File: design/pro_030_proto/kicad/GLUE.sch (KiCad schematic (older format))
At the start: 19 parts, among them IC10 74HCT93, IC11 74LS08, IC12 74HCT93, IC13 74HCT174, IC14 74LS01N, IC9 74174N, X2 8MHz

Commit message: Lots of work
* Sort out power and reset circuits, add ATX
* Add PCF8584 and supporting GAL code
* Stub out ATX board outline in PCB
* Various other tidying up and prep for layout
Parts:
- IC14: value 74LS01N -> 74LS05; symbol rosco_m68k-eagle-import:7401N -> 74xx:74LS05
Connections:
- wire segments 142 -> 139
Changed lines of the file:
@@
 $Descr A4 11693 8268
 encoding utf-8
-Sheet 6 13
+Sheet 6 15
 Title "rosco_m68k Pro (030) Prototype"
-Date "2021-07-24"
+Date "2021-10-01"
 Rev "0"
 Comp "The Really Old-School Company Limited"
@@
 	1950 750  1950 1150
 $Comp
-L rosco_m68k-eagle-import:7401N IC?
+L 74xx:74LS05 IC?
 U 4 1 60F552BD
-P 9950 1700
+P 9950 1600
 AR Path="/60F552BD" Ref="IC?"  Part="3"
 AR Path="/5E53B952/60F552BD" Ref="IC?"  Part="4"
 AR Path="/5E53BC83/60F552BD" Ref="IC?"  Part="4"
 AR Path="/60FBFA5C/60F552BD" Ref="IC14"  Part="4"
-F 0 "IC14" H 10050 1825 59  0000 L BNN
-F 1 "74LS01N" H 10050 1500 59  0001 L BNN
-F 2 "Package_DIP:DIP-14_W7.62mm_Socket_LongPads" H 9950 1700 50  0001 C CNN
-F 3 "" H 9950 1700 50  0001 C CNN
-	4    9950 1700
-	1    0    0    -1
-$EndComp
-Text GLabel 10250 1700 2    50   Output ~ 0
+F 0 "IC14" H 10050 1725 59  0000 L BNN
+F 1 "74LS05" H 10050 1400 59  0001 L BNN
+F 2 "Package_DIP:DIP-14_W7.62mm_Socket_LongPads" H 9950 1600 50  0001 C CNN
+F 3 "" H 9950 1600 50  0001 C CNN
+	4    9950 1600
+	1    0    0    -1
+$EndComp
+Text GLabel 10250 1600 2    50   Output ~ 0
 BERR
 Text Notes 9050 2600 2    50   ~ 0
 DTACK / IACK WATCHDOG
-Wire Wire Line
-	8550 2000 8550 2200
 $Comp
 L power:GND #PWR027
@@
 NoConn ~ 9050 1500
 NoConn ~ 9050 1400
-Connection ~ 9350 1600
-Wire Wire Line
-	9350 1600 9050 1600
-Wire Wire Line
-	9350 1800 9650 1800
-Wire Wire Line
-	9350 1600 9350 1800
-Wire Wire Line
-	9650 1600 9350 1600
 Text GLabel 8050 1300 0    50   Input ~ 0
 CLK_1M
@@
 Wire Wire Line
 	8050 3450 8050 4850
-Wire Wire Line
-	8050 5150 8600 5150
-Wire Wire Line
-	8600 5150 8600 4950
 $Comp
 L power:GND #PWR028
@@
 	1    0    0    -1
 $EndComp
-Connection ~ 8600 5150
 $Comp
 L power:VCC #PWR025
@@
 NoConn ~ 6100 6350
 NoConn ~ 6100 6950
+Wire Wire Line
+	9050 1600 9650 1600
+Wire Wire Line
+	8050 5150 8600 5150
+Wire Wire Line
+	8600 5150 8600 4950
+Connection ~ 8600 5150
+Wire Wire Line
+	8550 2200 8550 2000
 $EndSCHEMATC

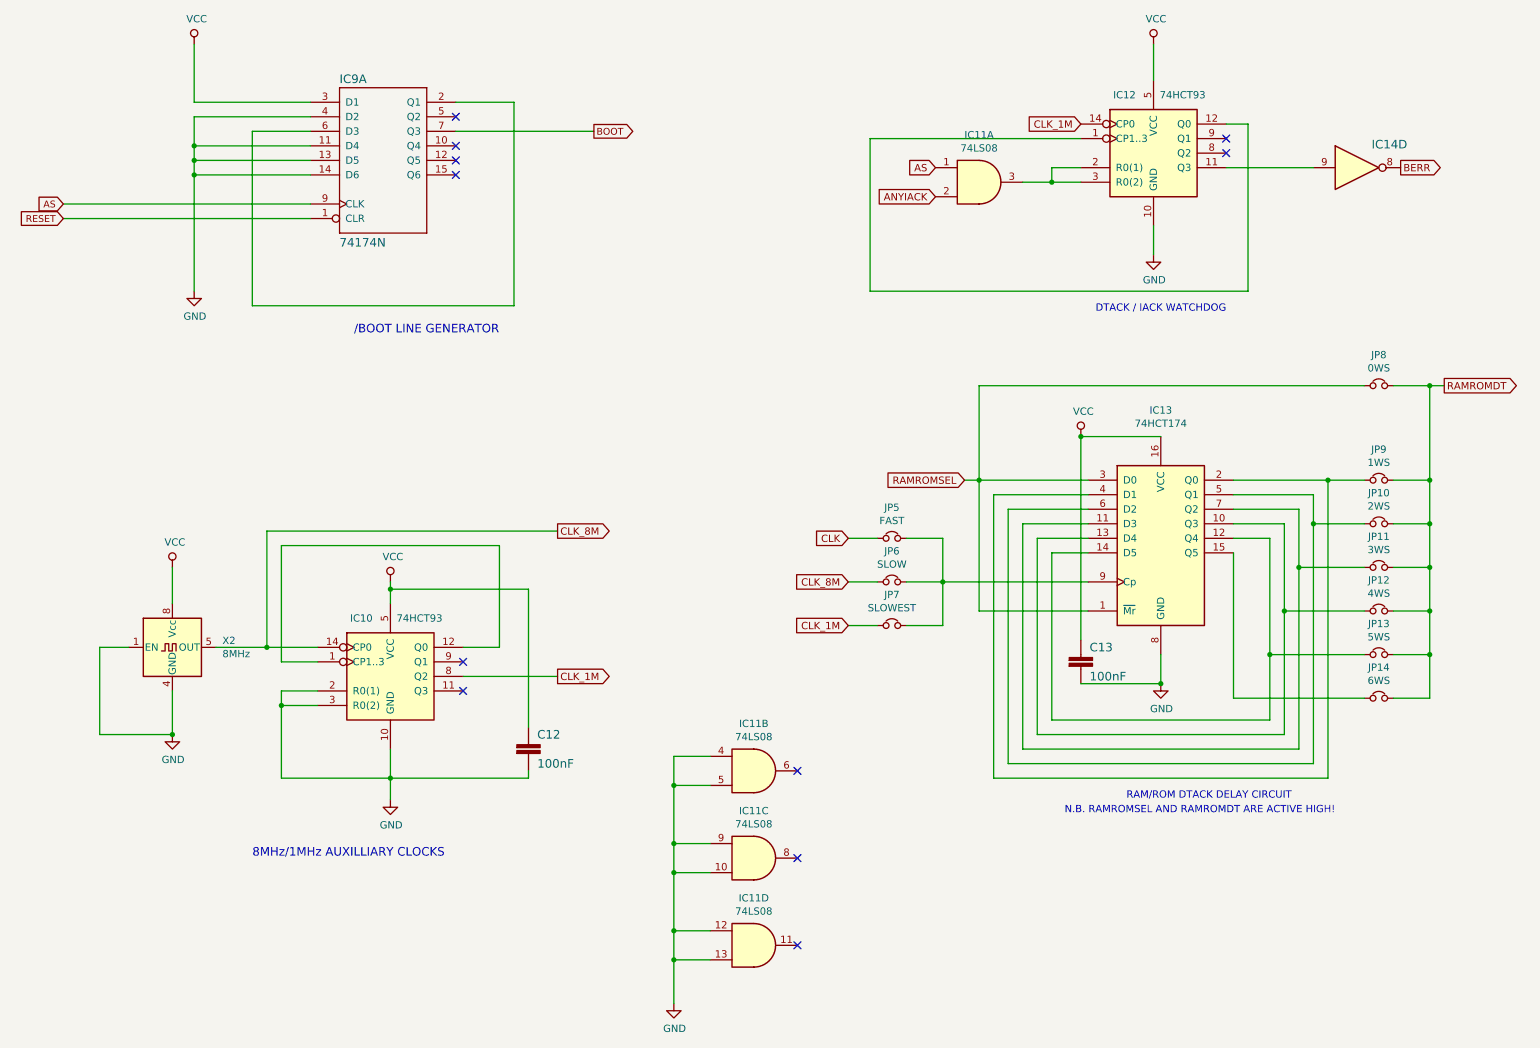
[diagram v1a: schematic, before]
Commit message: Replace 7493s and 7404 with IC10 GAL
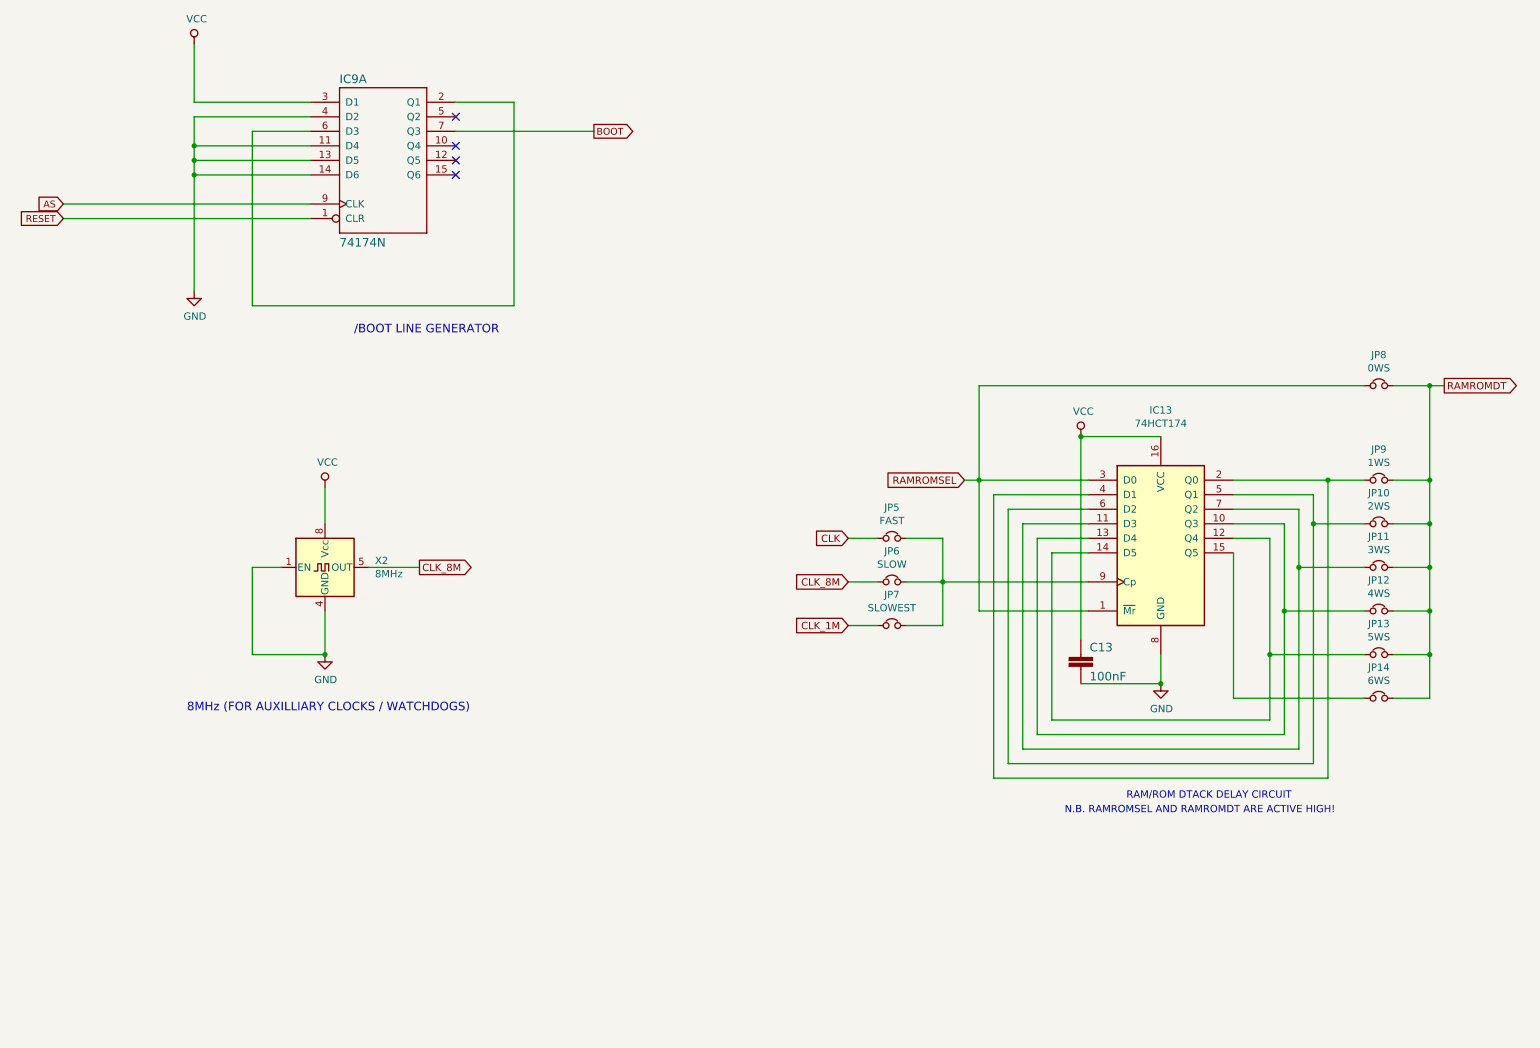
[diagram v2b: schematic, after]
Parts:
- removed C12: 100nF, Capacitor_THT:C_Rect_L4.0mm_W2.5mm_P2.50mm, symbol rosco_m68k-eagle-import:C2,5-3
- removed IC10, IC12: 74HCT93, Package_DIP:DIP-14_W7.62mm_Socket_LongPads, symbol 74xx:74LS93
- removed IC11: 74LS08, Package_DIP:DIP-14_W7.62mm_LongPads, symbol 74xx:74LS08
- removed IC14: 74LS05, Package_DIP:DIP-14_W7.62mm_Socket_LongPads, symbol 74xx:74LS05
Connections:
- no-connect marks 11 -> 4
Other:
- note added: "8MHz (FOR AUXILLIARY CLOCKS / WATCHDOGS)"
- note removed: "8MHz/1MHz AUXILLIARY CLOCKS"
- note removed: "DTACK / IACK WATCHDOG"
- moved on the sheet: X2

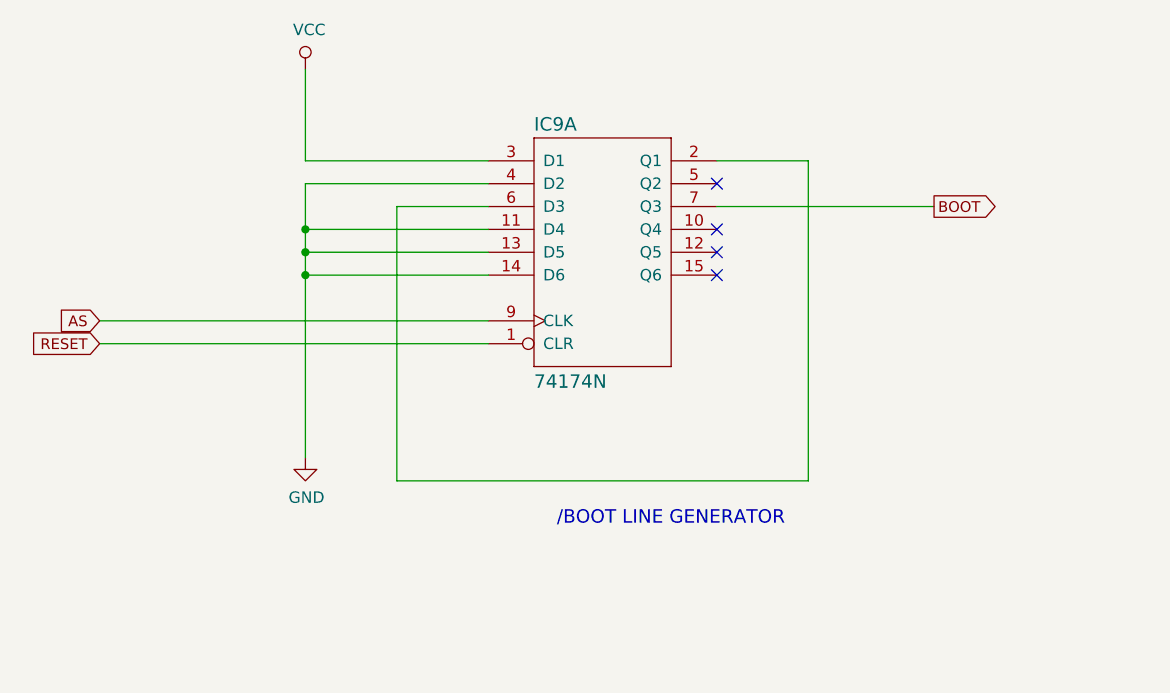
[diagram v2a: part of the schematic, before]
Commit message: Add IC14 GAL into schematic
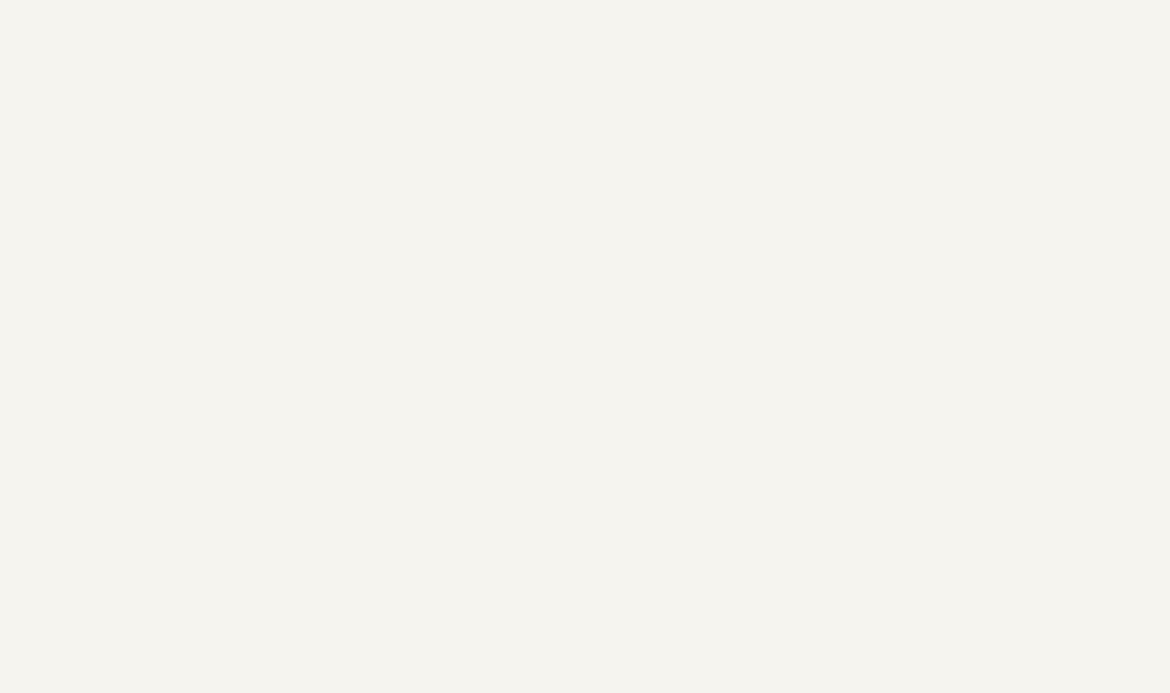
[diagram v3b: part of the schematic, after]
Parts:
- removed IC9: 74174N, Package_DIP:DIP-16_W7.62mm_Socket_LongPads, symbol rosco_m68k-eagle-import:74174N
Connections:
- no-connect marks 4 -> 0
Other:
- note removed: "/BOOT LINE GENERATOR"
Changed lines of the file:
@@
 Comment4 ""
 $EndDescr
-Wire Wire Line
-	1950 1150 2750 1150
-Wire Wire Line
-	2750 1250 1950 1250
-Wire Wire Line
-	1950 1250 1950 1450
-Wire Wire Line
-	2750 1550 1950 1550
-Connection ~ 1950 1550
-Wire Wire Line
-	4150 2550 2350 2550
-Wire Wire Line
-	2350 2550 2350 1350
-Wire Wire Line
-	2350 1350 2750 1350
-Wire Wire Line
-	3750 1150 4150 1150
-Wire Wire Line
-	4150 1150 4150 2550
-Text GLabel 4700 1350 2    47   Output ~ 0
-BOOT
-Wire Wire Line
-	2750 1850 1050 1850
-Text GLabel 1050 1850 0    47   Input ~ 0
-AS
-Wire Wire Line
-	2750 1950 1050 1950
-Text GLabel 1050 1950 0    47   Input ~ 0
-RESET
-$Comp
-L rosco_m68k-eagle-import:74174N IC?
-U 1 1 60F55293
-P 3250 1550
-AR Path="/60F55293" Ref="IC?"  Part="1"
-AR Path="/5E53B810/60F55293" Ref="IC?"  Part="1"
-AR Path="/5E53B952/60F55293" Ref="IC?"  Part="1"
-AR Path="/60FBFA5C/60F55293" Ref="IC9"  Part="1"
-F 0 "IC9" H 2950 2075 59  0000 L BNN
-F 1 "74174N" H 2950 950 59  0000 L BNN
-F 2 "Package_DIP:DIP-16_W7.62mm_Socket_LongPads" H 3250 1550 50  0001 C CNN
-F 3 "" H 3250 1550 50  0001 C CNN
-	1    3250 1550
-	1    0    0    -1
-$EndComp
-Text Notes 3050 2750 0    59   ~ 0
-/BOOT LINE GENERATOR
-NoConn ~ 3750 1250
-NoConn ~ 3750 1550
-$Comp
-L power:GND #PWR?
-U 1 1 60F5529C
-P 1950 2450
-AR Path="/5E53B810/60F5529C" Ref="#PWR?"  Part="1"
-AR Path="/5E53B952/60F5529C" Ref="#PWR?"  Part="1"
-AR Path="/60FBFA5C/60F5529C" Ref="#PWR021"  Part="1"
-F 0 "#PWR021" H 1950 2200 50  0001 C CNN
-F 1 "GND" H 1955 2277 50  0000 C CNN
-F 2 "" H 1950 2450 50  0001 C CNN
-F 3 "" H 1950 2450 50  0001 C CNN
-	1    1950 2450
-	1    0    0    -1
-$EndComp
-$Comp
-L power:VCC #PWR?
-U 1 1 60F552A2
-P 1950 750
-AR Path="/5E53B810/60F552A2" Ref="#PWR?"  Part="1"
-AR Path="/5E53B952/60F552A2" Ref="#PWR?"  Part="1"
-AR Path="/60FBFA5C/60F552A2" Ref="#PWR020"  Part="1"
-F 0 "#PWR020" H 1950 600 50  0001 C CNN
-F 1 "VCC" H 1967 923 50  0000 C CNN
-F 2 "" H 1950 750 50  0001 C CNN
-F 3 "" H 1950 750 50  0001 C CNN
-	1    1950 750
-	1    0    0    -1
-$EndComp
-Wire Wire Line
-	1950 1550 1950 1650
-Wire Wire Line
-	1950 750  1950 1150
 $Comp
 L 74xx:74LS174 IC13
@@
 Text Notes 9800 6050 2    50   ~ 0
 N.B. RAMROMSEL AND RAMROMDT ARE ACTIVE HIGH!
-Wire Wire Line
-	3750 1350 4700 1350
-Wire Wire Line
-	2750 1450 1950 1450
-Connection ~ 1950 1450
-Wire Wire Line
-	1950 1450 1950 1550
-Wire Wire Line
-	2750 1650 1950 1650
-Connection ~ 1950 1650
-Wire Wire Line
-	1950 1650 1950 2450
-NoConn ~ 3750 1450
-NoConn ~ 3750 1650
 $Comp
 L Device:Jumper_NC_Small JP5

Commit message: Fix some silly mistakes
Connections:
- net GND: no longer X2.1 (EN)
- net VCC: now also X2.1 (EN)
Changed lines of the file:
@@
 CLK_8M
 Wire Wire Line
-	2850 3800 2850 4050
-Connection ~ 2850 4950
+	2850 3800 2850 3950
 Wire Wire Line
 	2850 4650 2850 4950
-Wire Wire Line
-	2350 4950 2850 4950
-Wire Wire Line
-	2350 4350 2350 4950
 Wire Wire Line
 	2550 4350 2350 4350
@@
 Wire Wire Line
 	3150 4350 3500 4350
+Wire Wire Line
+	2350 4350 2350 3950
+Wire Wire Line
+	2350 3950 2850 3950
+Connection ~ 2850 3950
+Wire Wire Line
+	2850 3950 2850 4050
 $EndSCHEMATC
